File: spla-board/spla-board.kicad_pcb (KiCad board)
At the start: 4 copper layers, 178 x 107 mm, 283 parts, among them J1 USB_B_Micro, J12 J_POWER, J13 J_ANALOG, J14 J_AREF, J15 J_DPULL, J2 J_JTAG, J3 J_BODGE, J5 J_PPURESET, J6 J_SAMPLE, J7 Barrel_Jack, J8 J_AREF_AMP, J9 J_EXTRA, SW1 PTS645, U1 LFE5U-45F-BG256, U10 SNES_PPU1, U11 SNES_PPU2, U12 VRAM, U13 VRAM, U14 TLV73311PDBV, U15 74LVC8T245, U16 74LVC8T245, U17 74LVC8T245, U2 FT2232H, U20 74LVC8T245, U22 74LVC8T245, U23 74LVC8T245, U24 74LVC8T245, U25 74LVC8T245, U26 74LVC8T245, U27 74LVC8T245, U28 74LVC8T245, U29 74LVC8T245, U3 93LC66B, U30 74LVC8T245, U31 74LVC8T245, U32 74LVC8T245, U4 74LVC1G17, U5 74LVC1G17, U51 ADC1173, U52 ADC1173, U53 ADC1173, U61 LMH6611, U62 LMH6611, U63 LMH6611, U7 ST1S10PHR, U74 LMH6611, U75 LMH6611, U76 TLV73333PDBV, U8 ST1S10PHR, U9 TLV73325PDBV, X1 FT5HNBPK12.0-T1

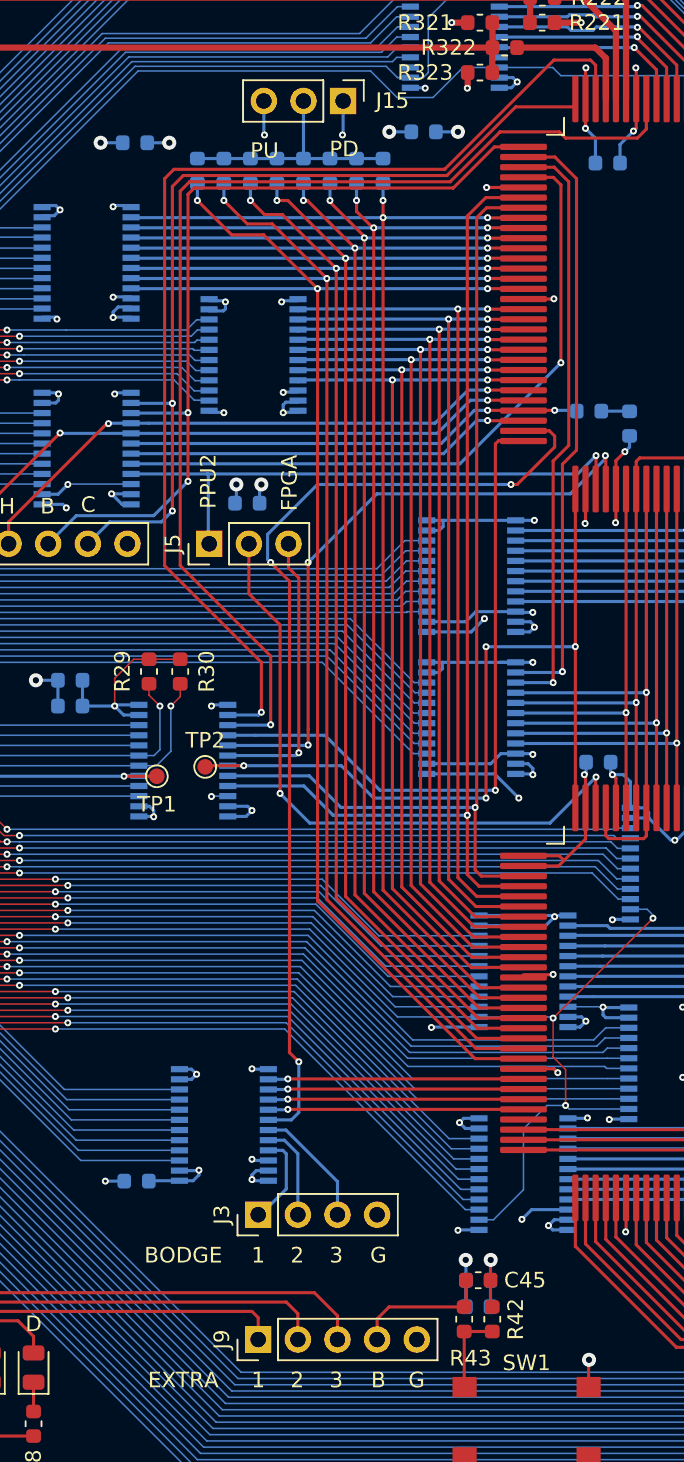
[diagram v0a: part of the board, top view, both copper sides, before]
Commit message: pcb: Rearrange power plane splits; tweak bulk decoupling.
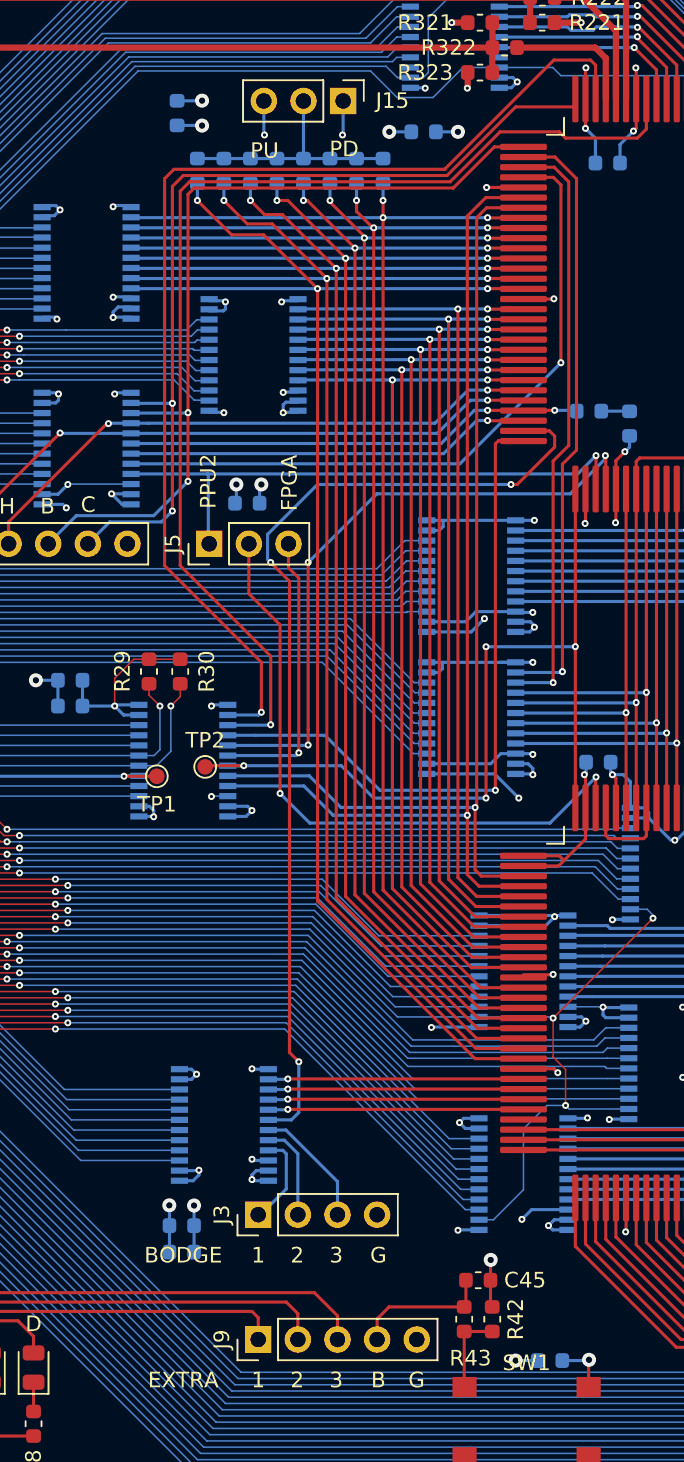
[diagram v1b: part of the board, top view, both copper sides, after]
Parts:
- moved C26 28.9 mm to (158.7, 144.3)
- moved C14 19.3 mm to (135.1, 137.4)
- moved C28 19.3 mm to (135.1, 135.7)
- moved C22 3.30 mm to (134.8, 64.4), turned to 90 degrees
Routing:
- net +5V: track 322.0 -> 288.3 mm
- net +3V3: track 162.8 -> 158.1 mm
- net GND: track 522.5 -> 522.9 mm, vias 161 -> 162

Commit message: schematic/pcb: Add jumper for button.
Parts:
- added BOM25: Jumper, SPLA:BoM, F.Cu at (56.0, 184.0)

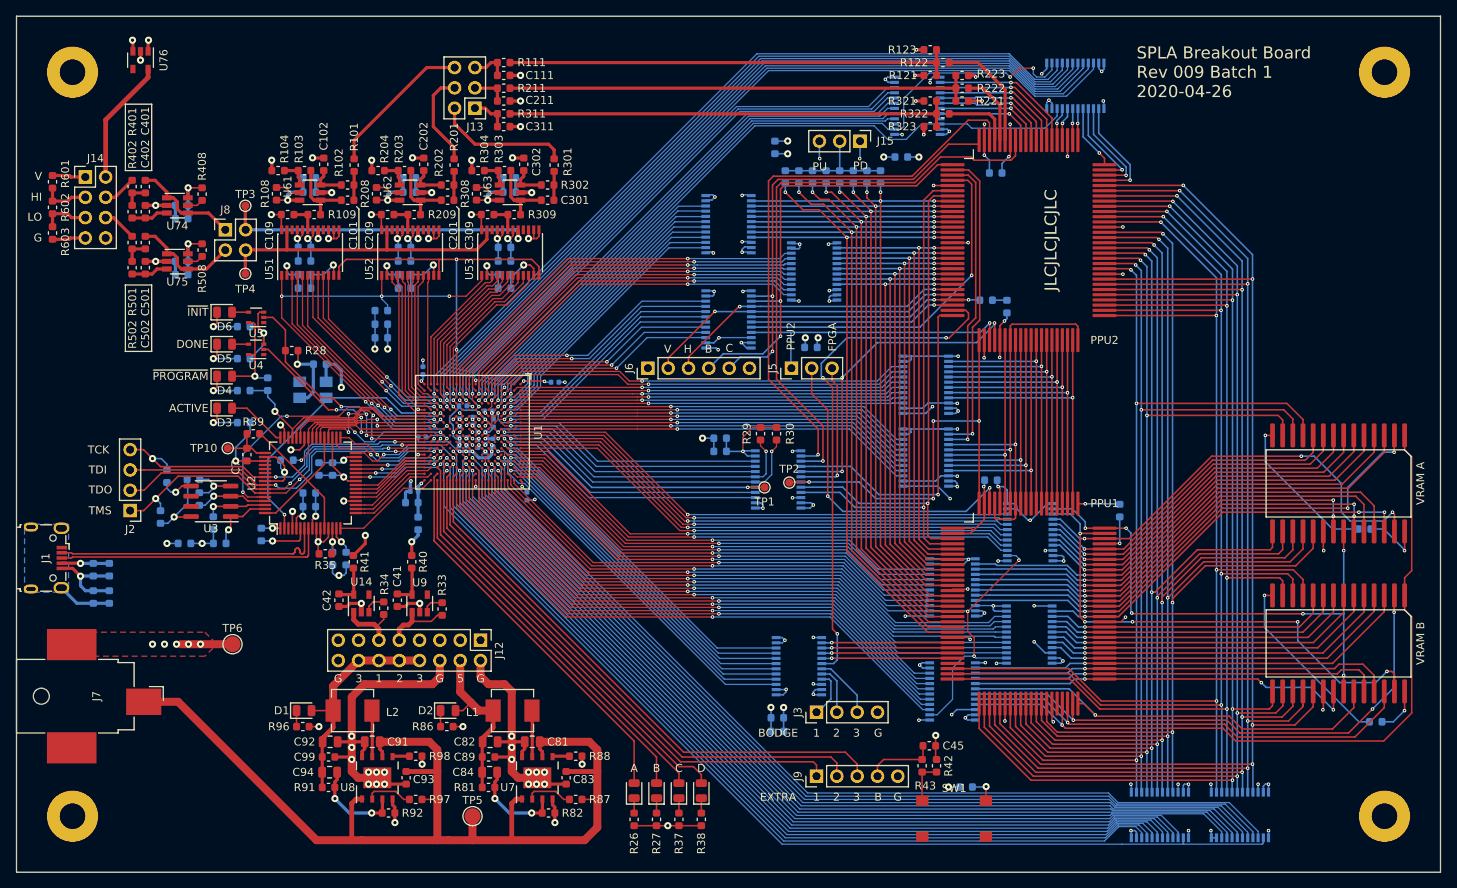
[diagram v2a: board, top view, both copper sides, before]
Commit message: pcb: Compact left side of board by 13mm.
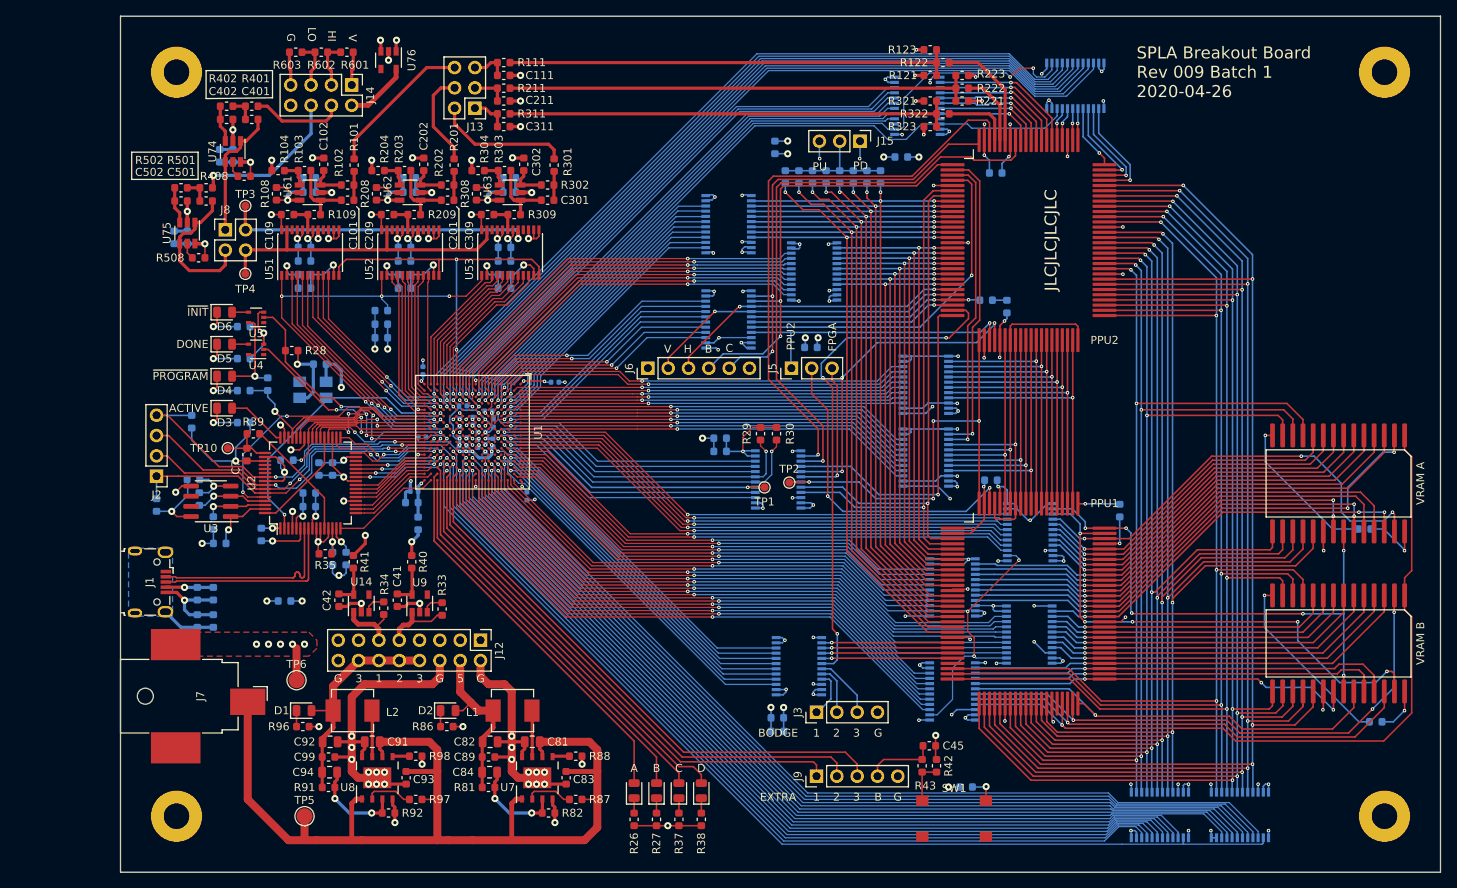
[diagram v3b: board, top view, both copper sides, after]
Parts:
- moved R601 40.2 mm to (81.3, 52.5), turned to 180 degrees
- moved R602 38.8 mm to (78.1, 52.5), turned to 180 degrees
- moved R603 37.9 mm to (74.9, 52.5), turned to 180 degrees
- moved J14 35.2 mm to (81.9, 56.6), turned to 270 degrees
- moved U76 31.0 mm to (86.5, 53.5)
- moved TP5 21.0 mm to (76.0, 148.0)
- moved R401 18.0 mm to (69.4, 59.2), turned to 180 degrees
- moved R402 17.7 mm to (66.3, 59.2), turned to 180 degrees
- moved C401 15.7 mm to (69.4, 60.9), turned to 180 degrees
- moved C402 15.4 mm to (66.3, 60.9), turned to 0 degrees
- moved C16 14.4 mm to (73.5, 121.1)
- moved C1 13.3 mm to (62.6, 120.2)
- moved J1 13.3 mm to (56.8, 118.7)
- moved R32 13.3 mm to (62.6, 123.6)
- moved C44 13.3 mm to (64.6, 123.6)
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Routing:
- net Net-(J14-Pad6): track 4.28 -> 19.5 mm, vias 0 -> 1
- net /SPLA Board - USB/USB_D+: track 34.3 -> 24.3 mm
- net /SPLA Board - USB/USB_D-: track 34.3 -> 24.3 mm
- net /SPLA Board - Analog/3.3VA_IN: track 15.7 -> 8.05 mm
- net Net-(J14-Pad4): track 4.19 -> 11.5 mm
- net +12V: track 132.2 -> 126.3 mm
- net /SPLA Board - Analog/AREF_LO_OP: track 13.6 -> 18.5 mm
- net JTAG_TMS: track 44.7 -> 40.6 mm, vias 3 -> 2
- net GND: track 522.9 -> 526.5 mm
- net JTAG_TDO: track 45.2 -> 41.9 mm
- net /SPLA Board - Analog/AREF_HI_OP: track 13.5 -> 16.4 mm
- net JTAG_TDI: track 41.8 -> 40.3 mm
- net +3V3: track 158.1 -> 158.0 mm, vias 49 -> 50
- net JTAG_TCK: vias 3 -> 2
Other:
- board size 178 x 107 mm -> 165 x 107 mm
- board text removed: "TCK"
- board text removed: "TDI"
- board text removed: "TDO"
- board text removed: "TMS"

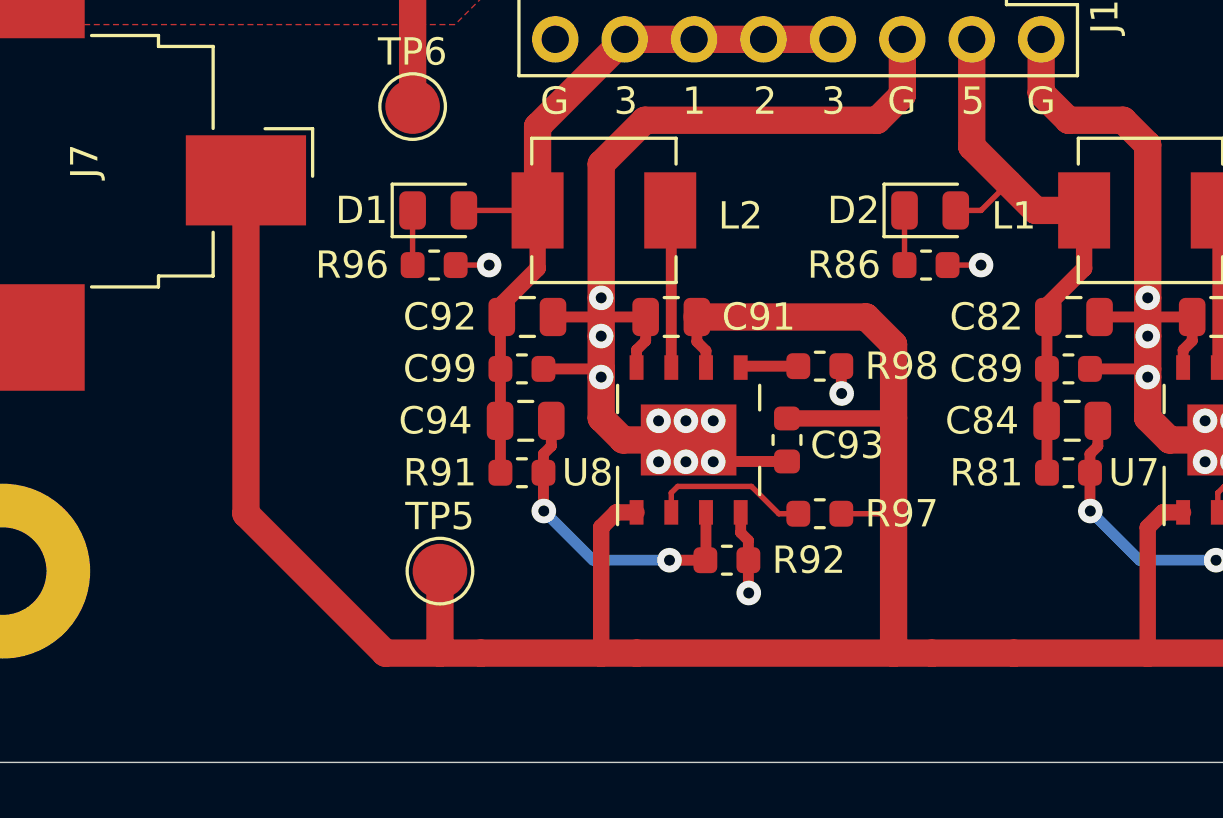
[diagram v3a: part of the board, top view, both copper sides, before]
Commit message: schematic/pcb: Add discrete power switch.
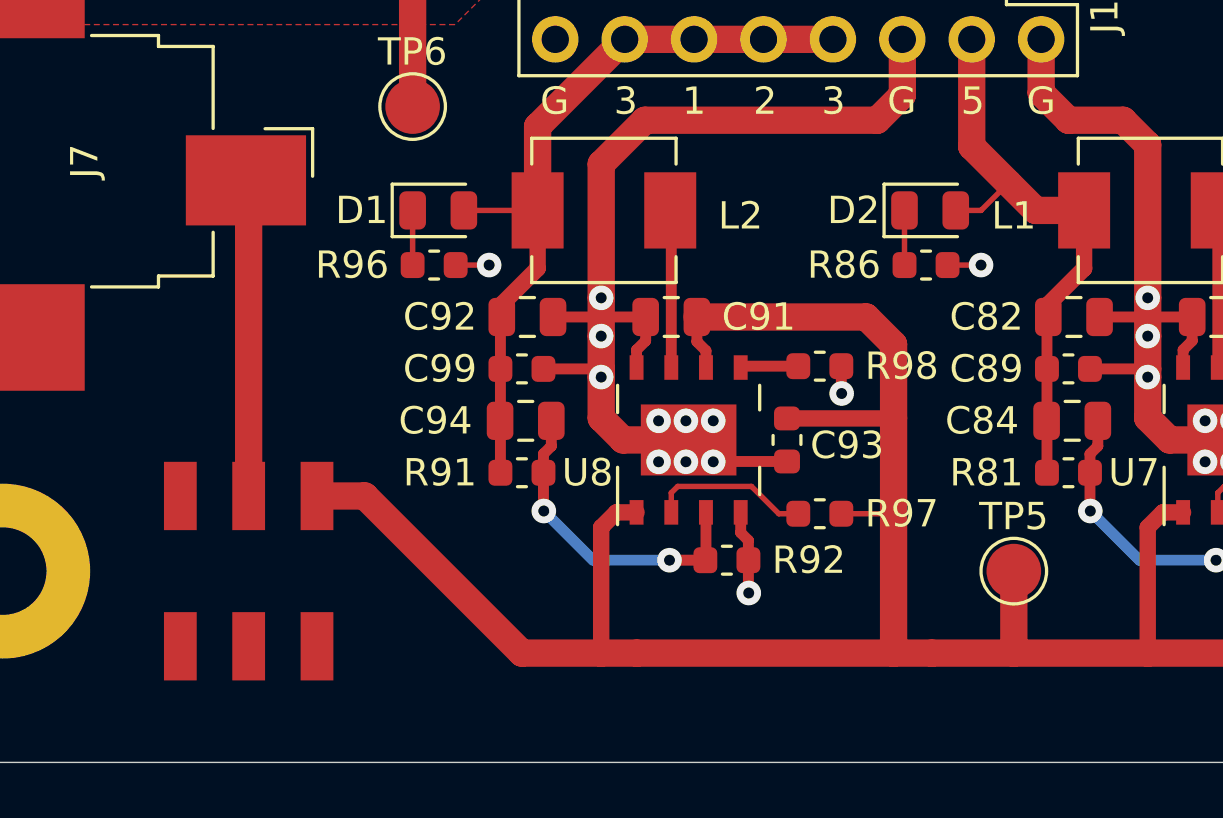
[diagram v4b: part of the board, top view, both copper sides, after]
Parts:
- added SW2: SW_DPDT_x2, SPLA:JS202011SCQN, F.Cu at (69.0, 148.0)
- moved TP5 21.0 mm to (97.0, 148.0)
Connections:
- J7 pad 1: +12V -> /SPLA Board - Power/PWR_12V_IN
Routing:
- net +12V: track 126.3 -> 111.2 mm
- net /SPLA Board - Power/PWR_12V_IN: track 0.00 -> 11.6 mm

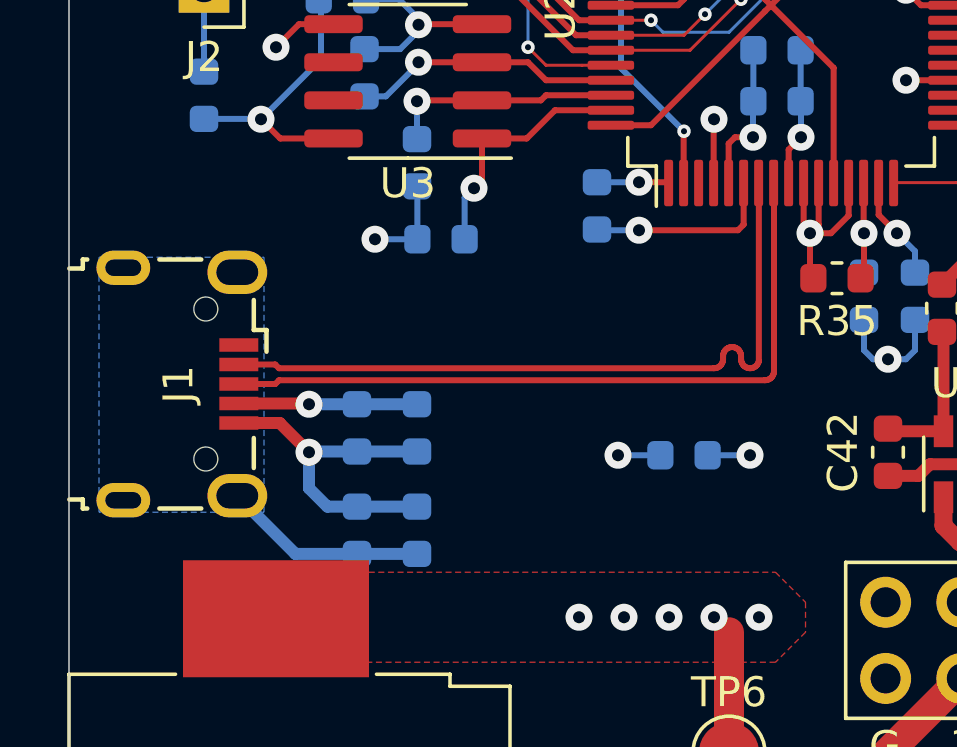
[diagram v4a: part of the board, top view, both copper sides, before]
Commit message: pcb: Move USB connector slightly away from power jack.
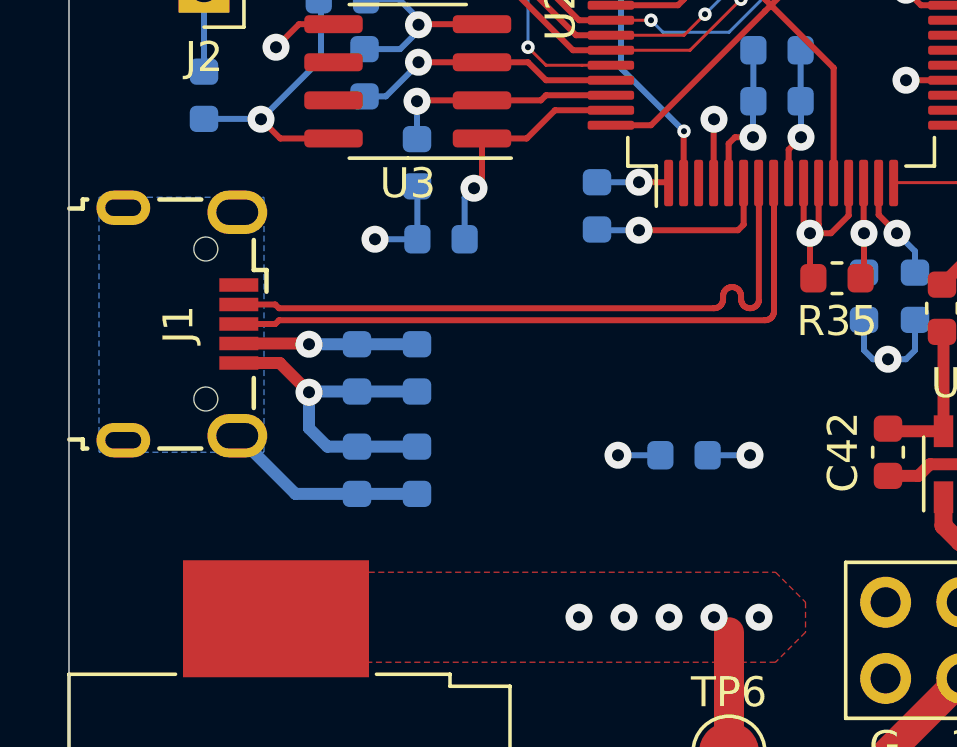
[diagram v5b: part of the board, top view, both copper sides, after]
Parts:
- moved C1 2.00 mm to (62.6, 118.2)
- moved C44 2.00 mm to (64.6, 121.6)
- moved J1 2.00 mm to (56.8, 116.7)
- moved R1 2.00 mm to (64.6, 118.2)
- moved R32 2.00 mm to (62.6, 121.6)
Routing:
- net /SPLA Board - USB/USB_D-: track 24.3 -> 22.3 mm
- net /SPLA Board - USB/USB_D+: track 24.3 -> 22.3 mm
